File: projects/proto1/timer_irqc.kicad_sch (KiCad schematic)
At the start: 6 parts, among them J11 TIMER0-3, J12 TIMER4-7, U45 74LS348, U46 MC68901P, U47 MC68901P

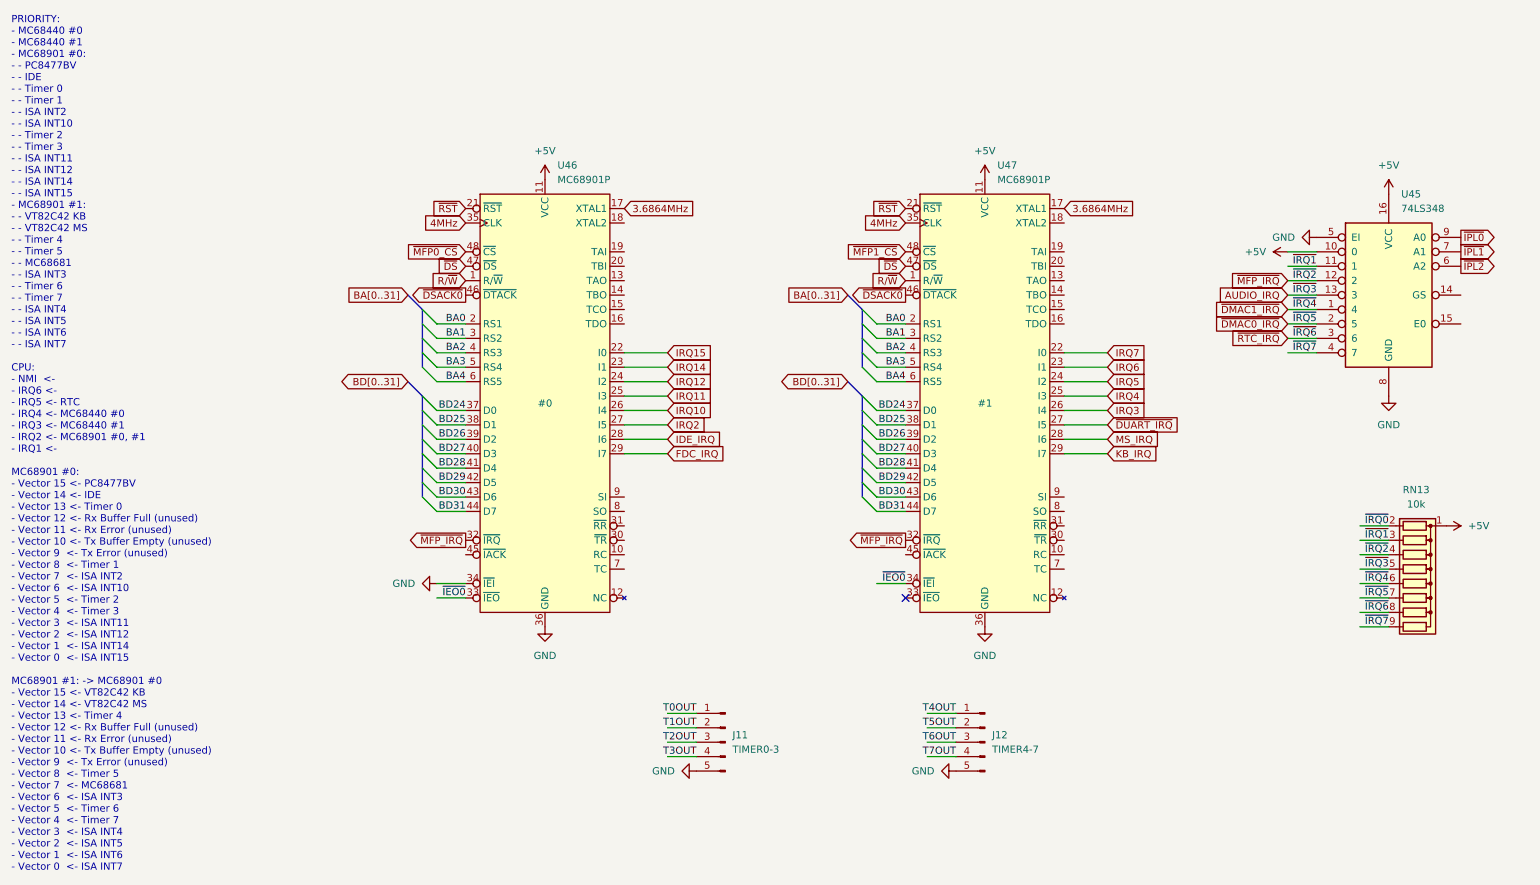
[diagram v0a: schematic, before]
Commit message: Renamed CMC to SCU, changed verification method to cocotb, and modified pcb schematic
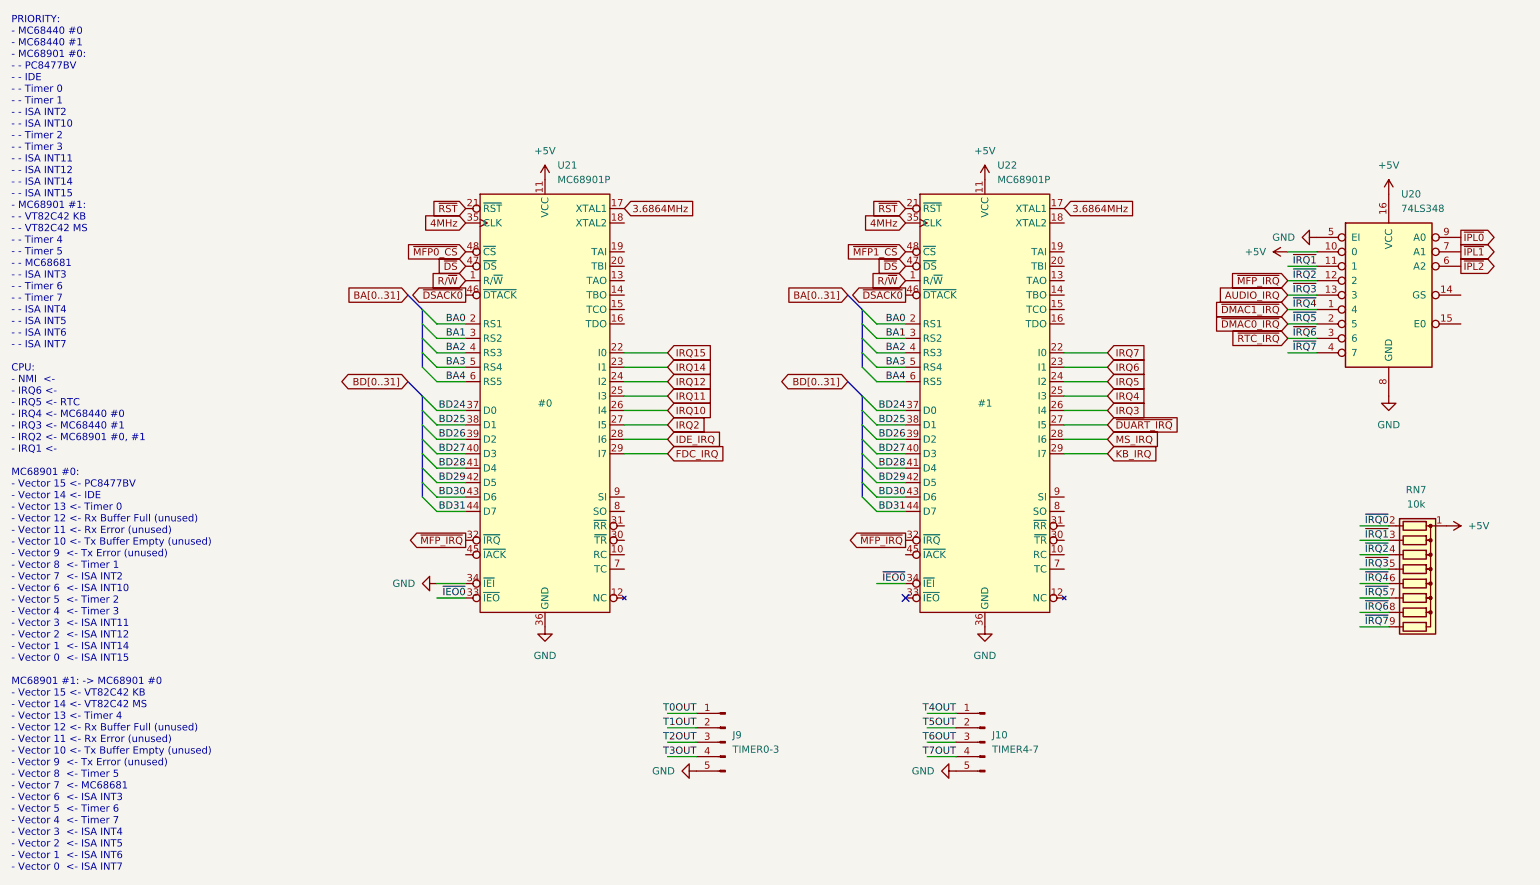
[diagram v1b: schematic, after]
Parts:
- renumbered J12 to J10, J11 to J9, RN13 to RN7, U45 to U20, U46 to U21, U47 to U22

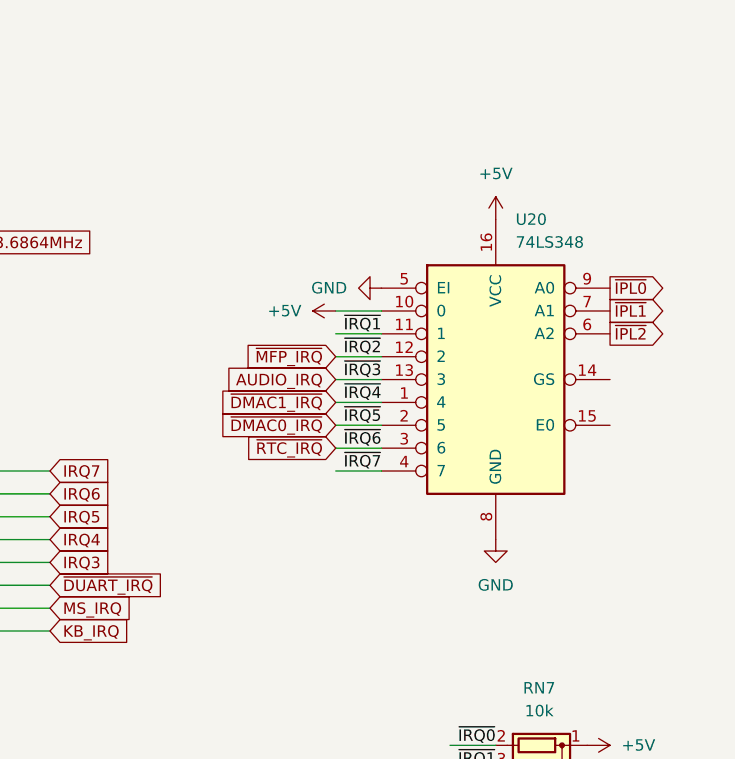
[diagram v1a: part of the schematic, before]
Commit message: Added timer and interrupt controller capability to SCU
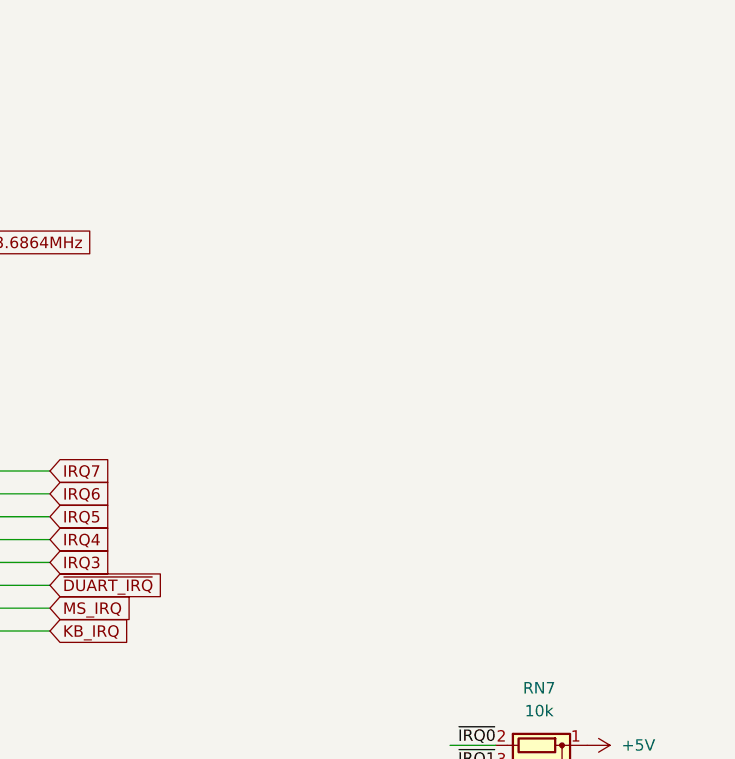
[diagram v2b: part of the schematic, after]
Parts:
- removed U20: 74LS348, Package_DIP:DIP-16_W7.62mm_Socket, symbol 74xx:74LS348
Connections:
- net ~{MFP_IRQ}: no longer RN7.4 (R3)
- net AUDIO_IRQ renamed ~{IRQ3}
- net ~{DMAC0_IRQ} renamed ~{IRQ5}
- net ~{DMAC1_IRQ} renamed ~{IRQ4}
- net ~{RTC_IRQ} renamed ~{IRQ6}
- new net ~{IRQ2}: RN7.4 (R3)
